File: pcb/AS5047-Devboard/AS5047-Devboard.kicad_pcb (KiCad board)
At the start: 2 copper layers, 42 x 42 mm, 8 parts, among them J1 SPI_CONN, U1 AS5047P

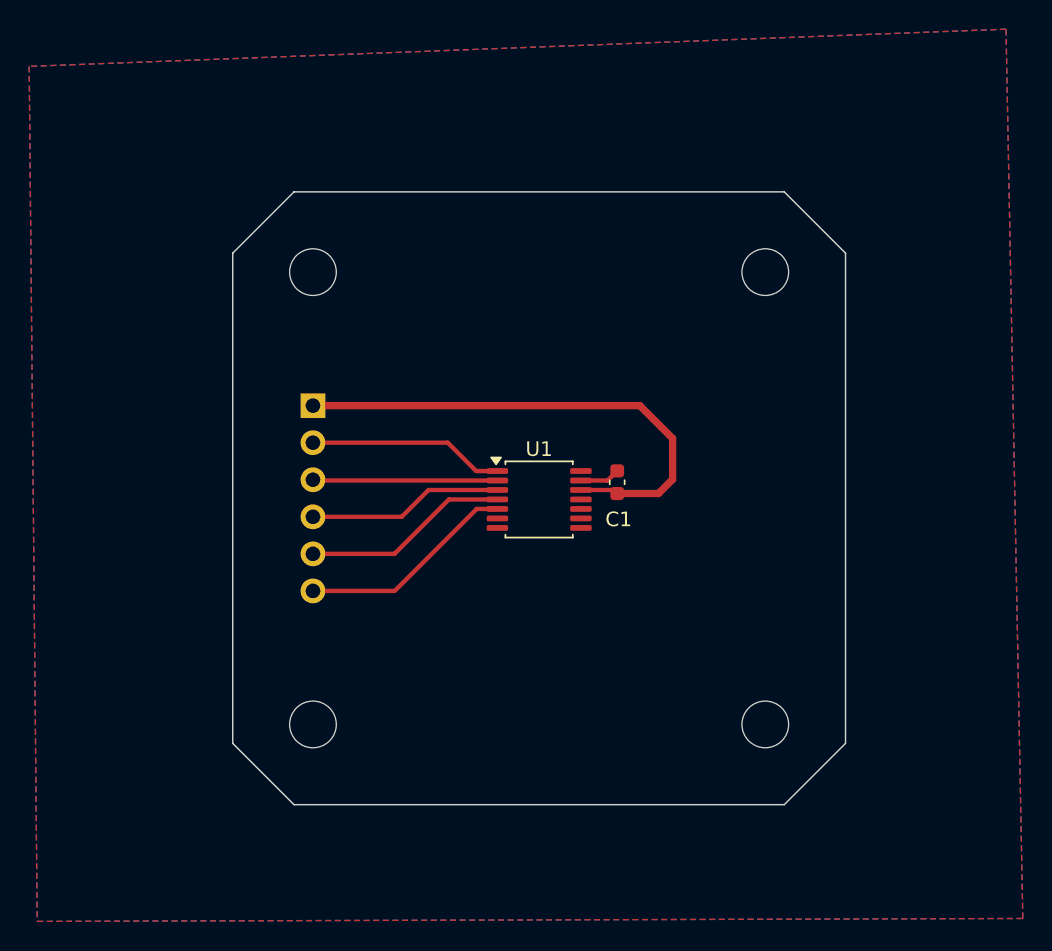
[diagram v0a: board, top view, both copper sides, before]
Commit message: updated AS5047P board to include stitching vias
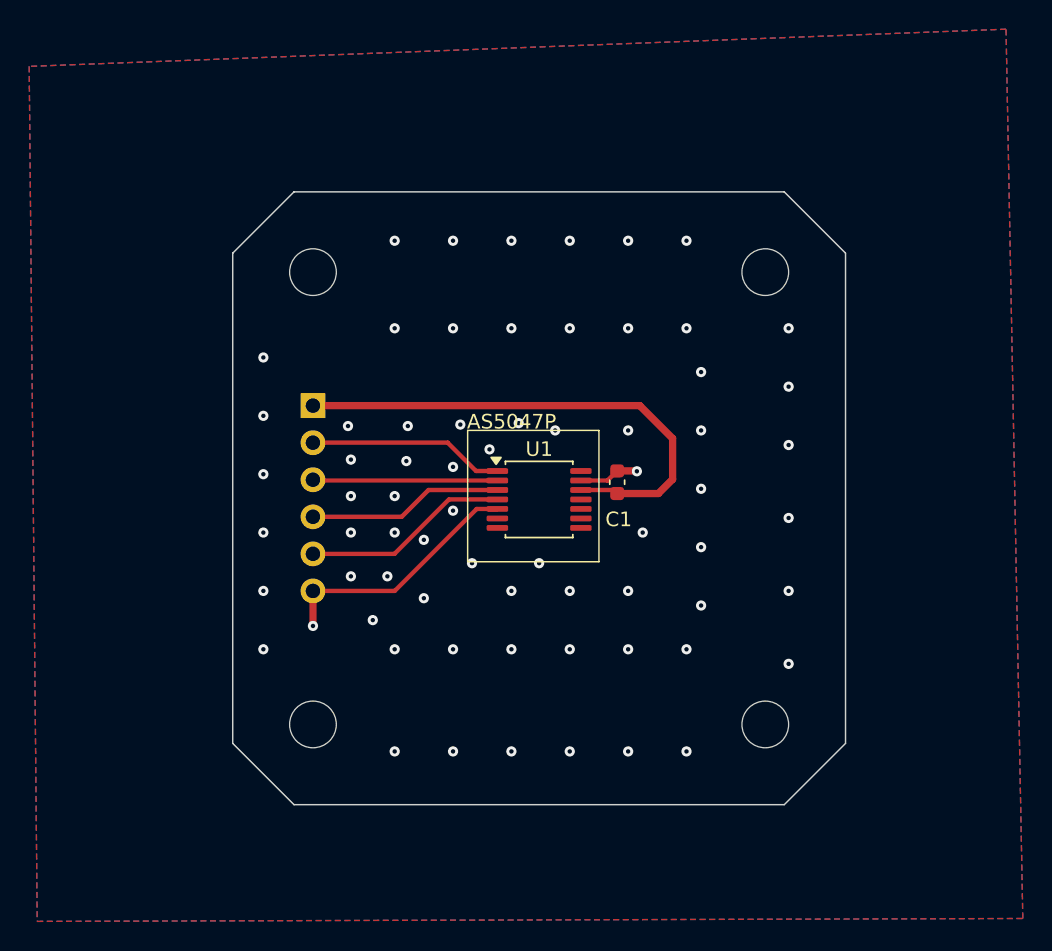
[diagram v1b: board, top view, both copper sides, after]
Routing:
- net GND: track 17.7 -> 21.5 mm, vias 0 -> 69
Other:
- board text added: "AS5047P"

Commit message: updated BOM
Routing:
- net GND: vias 69 -> 75
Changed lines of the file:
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@@
 			(drillshape 0)
 			(scaleselection 1)
-			(outputdirectory "")
+			(outputdirectory "manufacturing/")
 		)
 	)
@@
 	)
 	(via
+		(at 157.25 107.75)
+		(size 0.6)
+		(drill 0.3)
+		(layers "F.Cu" "B.Cu")
+		(free yes)
+		(net 6)
+	)
+	(via
 		(at 166 123)
 		(size 0.7)
@@
 	)
 	(via
+		(at 157.25 103.75)
+		(size 0.6)
+		(drill 0.3)
+		(layers "F.Cu" "B.Cu")
+		(free yes)
+		(net 6)
+	)
+	(via
 		(at 166 94)
 		(size 0.7)
@@
 	)
 	(via
+		(at 154.75 103.75)
+		(size 0.6)
+		(drill 0.3)
+		(layers "F.Cu" "B.Cu")
+		(free yes)
+		(net 6)
+	)
+	(via
 		(at 150 88)
 		(size 0.7)
@@
 	)
 	(via
+		(at 154.75 107.75)
+		(size 0.6)
+		(drill 0.3)
+		(layers "F.Cu" "B.Cu")
+		(free yes)
+		(net 6)
+	)
+	(via
 		(at 162 101)
 		(size 0.7)
@@
 	)
 	(via
+		(at 157.25 105.75)
+		(size 0.6)
+		(drill 0.3)
+		(layers "F.Cu" "B.Cu")
+		(free yes)
+		(net 6)
+	)
+	(via
 		(at 173 117)
 		(size 0.7)
@@
 		(drill 0.3)
 		(layers "F.Cu" "B.Cu")
+		(free yes)
+		(net 6)
+	)
+	(via
+		(at 154.75 105.75)
+		(size 0.6)
+		(drill 0.3)
+		(layers "F.Cu" "B.Cu")

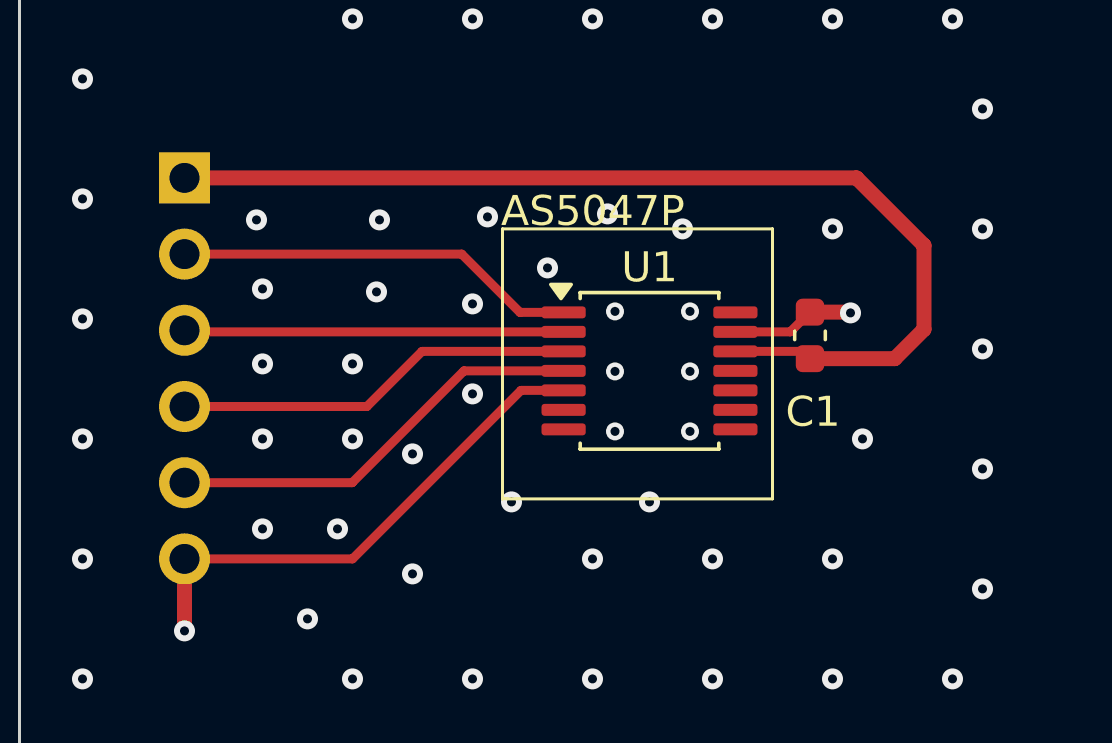
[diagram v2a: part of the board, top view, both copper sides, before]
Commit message: Updated sensor coorindates for AS5047P
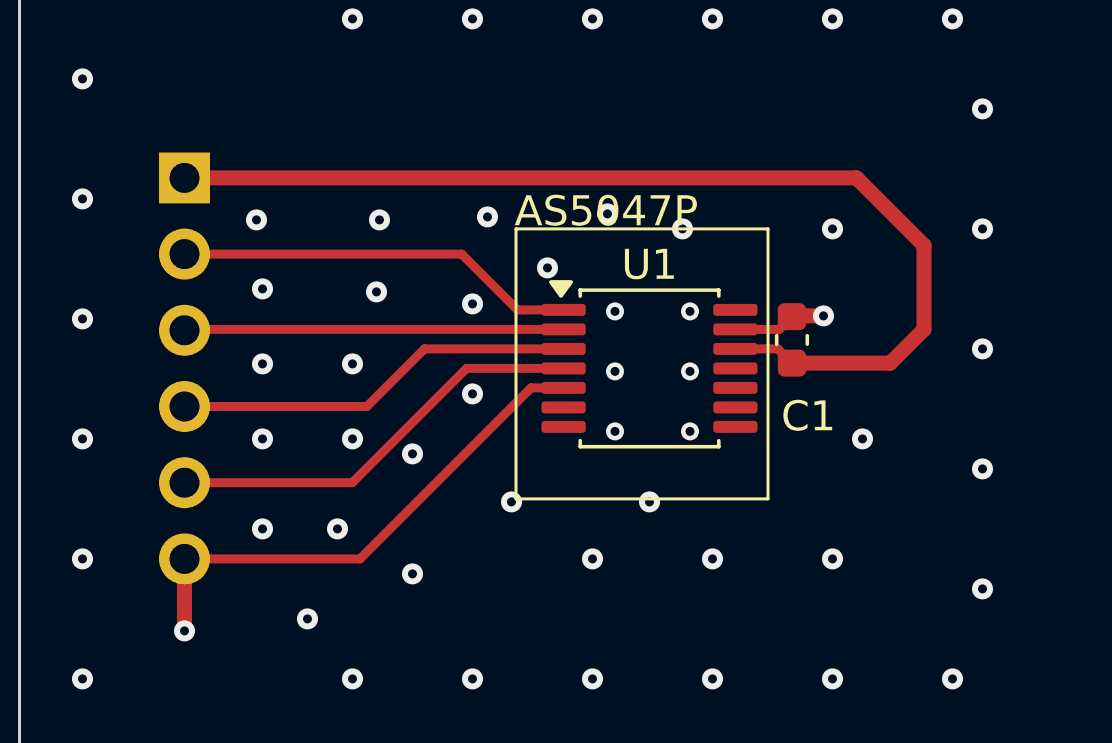
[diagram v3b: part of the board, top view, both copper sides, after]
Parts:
- moved C1 0.62 mm to (160.7, 104.7)
- moved U1 0.08 mm to (155.9, 105.7)
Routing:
- net GND: track 21.5 -> 20.4 mm
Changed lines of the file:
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@@
 	(footprint "Package_SO:TSSOP-14_4.4x5mm_P0.65mm"
 		(layer "F.Cu")
-		(at 155.9 105.7325)
+		(at 155.9 105.65)
 		(descr "TSSOP, 14 Pin (JEDEC MO-153 variation AB-1, 1.00mm body thickness, https://www.jedec.org/document_search?search_api_views_fulltext=MO-153), generated with kicad-footprint-generator ipc_gullwing_generator.py")
 		(tags "TSSOP SO")
@@
 	(footprint "Capacitor_SMD:C_0603_1608Metric"
 		(layer "F.Cu")
-		(at 161.25 104.55 90)
+		(at 160.65 104.7 90)
 		(descr "Capacitor SMD 0603 (1608 Metric), square (rectangular) end terminal, IPC-7351 nominal, (Body size source: IPC-SM-782 page 76, https://www.pcb-3d.com/wordpress/wp-content/uploads/ipc-sm-782a_amendment_1_and_2.pdf), generated with kicad-footprint-generator")
 		(tags "capacitor")
 		(property "Reference" "C1"
-			(at -2.55 0.1 180)
+			(at -2.55 0.55 180)
 			(layer "F.SilkS")
 			(effects
@@
 	)
 	(gr_rect
-		(start 151 101)
-		(end 160 110)
+		(start 151.45 101)
+		(end 159.85 110)
 		(stroke
 			(width 0.1)
@@
 	)
 	(gr_text "AS5047P"
-		(at 150.95 100.99 0)
+		(at 151.4 101 0)
 		(layer "F.SilkS" knockout)
 		(effects
@@
 	)
 	(segment
-		(start 148.3175 105.0825)
+		(start 148.4 105)
 		(end 146.48 106.92)
 		(width 0.3)
@@
 	)
 	(segment
-		(start 153.0375 105.0825)
-		(end 148.3175 105.0825)
+		(start 152.955 105)
+		(end 148.4 105)
 		(width 0.3)
 		(layer "F.Cu")
 		(net 1)
-	)
-	(segment
-		(start 151.5825 103.7825)
-		(end 149.64 101.84)
-		(width 0.3)
-		(layer "F.Cu")
-		(net 2)
-	)
-	(segment
-		(start 153.0375 103.7825)
-		(end 151.5825 103.7825)
-		(width 0.3)
-		(layer "F.Cu")
-		(net 2)
 	)
 	(segment
@@
 	)
 	(segment
+		(start 152.955 103.7)
+		(end 151.5 103.7)
+		(width 0.3)
+		(layer "F.Cu")
+		(net 2)
+	)
+	(segment
+		(start 151.5 103.7)
+		(end 149.64 101.84)
+		(width 0.3)
+		(layer "F.Cu")
+		(net 2)
+	)
+	(segment
 		(start 140.4525 104.4325)
 		(end 140.4 104.38)
@@
 	)
 	(segment
-		(start 153.0375 104.4325)
-		(end 140.4525 104.4325)
+		(start 140.43 104.35)
+		(end 140.4 104.38)
 		(width 0.3)
 		(layer "F.Cu")
@@
 	)
 	(segment
-		(start 164.075 105.325)
-		(end 161.25 105.325)
-		(width 0.5)
-		(layer "F.Cu")
-		(net 4)
-	)
-	(segment
-		(start 165.05 104.35)
-		(end 164.075 105.325)
+		(start 153.0375 104.35)
+		(end 140.43 104.35)
+		(width 0.3)
+		(layer "F.Cu")
+		(net 3)
+	)
+	(segment
+		(start 163.925 105.475)
+		(end 160.65 105.475)
 		(width 0.5)
 		(layer "F.Cu")
@@
 	)
 	(segment
-		(start 158.7625 105.0825)
-		(end 161.0075 105.0825)
+		(start 160.175 105)
+		(end 160.65 105.475)
+		(width 0.3)
+		(layer "F.Cu")
+		(net 4)
+	)
+	(segment
+		(start 158.7625 105)
+		(end 160.175 105)
 		(width 0.3)
 		(layer "F.Cu")
@@
 	)
 	(segment
-		(start 161.0075 105.0825)
-		(end 161.25 105.325)
-		(width 0.3)
+		(start 165.05 104.35)
+		(end 163.925 105.475)
+		(width 0.5)
 		(layer "F.Cu")
 		(net 4)
@@
 	)
 	(segment
+		(start 152.955 105.65)
+		(end 149.8 105.65)
+		(width 0.3)
+		(layer "F.Cu")
+		(net 5)
+	)
+	(segment
+		(start 149.8 105.65)
+		(end 145.99 109.46)
+		(width 0.3)
+		(layer "F.Cu")
+		(net 5)
+	)
+	(segment
 		(start 145.99 109.46)
 		(end 140.4 109.46)
@@
 	)
 	(segment
-		(start 153.0375 105.7325)
-		(end 149.7175 105.7325)
-		(width 0.3)
-		(layer "F.Cu")
-		(net 5)
-	)
-	(segment
-		(start 149.7175 105.7325)
-		(end 145.99 109.46)
-		(width 0.3)
-		(layer "F.Cu")
-		(net 5)
-	)
-	(segment
-		(start 146 112)
-		(end 151.6175 106.3825)
-		(width 0.3)
-		(layer "F.Cu")
-		(net 6)
-	)
-	(segment
 		(start 140.4 112)
 		(end 140.4 114.4)
@@
 	)
 	(segment
+		(start 146.25 112)
+		(end 151.95 106.3)
+		(width 0.3)
+		(layer "F.Cu")
+		(net 6)
+	)
+	(segment
 		(start 140.4 112)
-		(end 146 112)
+		(end 146.25 112)
 		(width 0.3)
 		(layer "F.Cu")
@@
 	)
 	(segment
-		(start 162.575 103.775)
-		(end 162.6 103.8)
+		(start 158.7625 104.35)
+		(end 160.225 104.35)
 		(width 0.3)
 		(layer "F.Cu")
@@
 	)
 	(segment
-		(start 151.6175 106.3825)
-		(end 153.0375 106.3825)
+		(start 151.95 106.3)
+		(end 152.955 106.3)
 		(width 0.3)
 		(layer "F.Cu")
@@
 	)
 	(segment
-		(start 161.25 103.775)
-		(end 162.575 103.775)
+		(start 160.225 104.35)
+		(end 160.65 103.925)
+		(width 0.3)
+		(layer "F.Cu")
+		(net 6)
+	)
+	(segment
+		(start 161.7 103.9)
+		(end 160.675 103.9)
 		(width 0.5)
 		(layer "F.Cu")
@@
 	)
 	(segment
-		(start 158.7625 104.4325)
-		(end 160.5925 104.4325)
-		(width 0.3)
-		(layer "F.Cu")
-		(net 6)
-	)
-	(segment
-		(start 160.5925 104.4325)
-		(end 161.25 103.775)
-		(width 0.3)
+		(start 160.675 103.9)
+		(end 160.65 103.925)
+		(width 0.5)
 		(layer "F.Cu")
 		(net 6)
@@
 	)
 	(via
-		(at 162.6 103.8)
+		(at 161.7 103.9)
 		(size 0.7)
 		(drill 0.3)
@@
 		(filled_areas_thickness no)
 		(keepout
-			(tracks not_allowed)
+			(tracks allowed)
 			(vias not_allowed)
 			(pads not_allowed)
@@
 		(polygon
 			(pts
-				(xy 159.45 104.2) (xy 160.25 104.05) (xy 160.5 104.75) (xy 159.45 104.7)
-			)
-		)
+				(xy 159.4 103.95) (xy 160.1 103.85) (xy 160.2 104.6) (xy 159.45 104.7)
+			)
+		)
